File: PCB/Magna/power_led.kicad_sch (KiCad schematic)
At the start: 10 parts

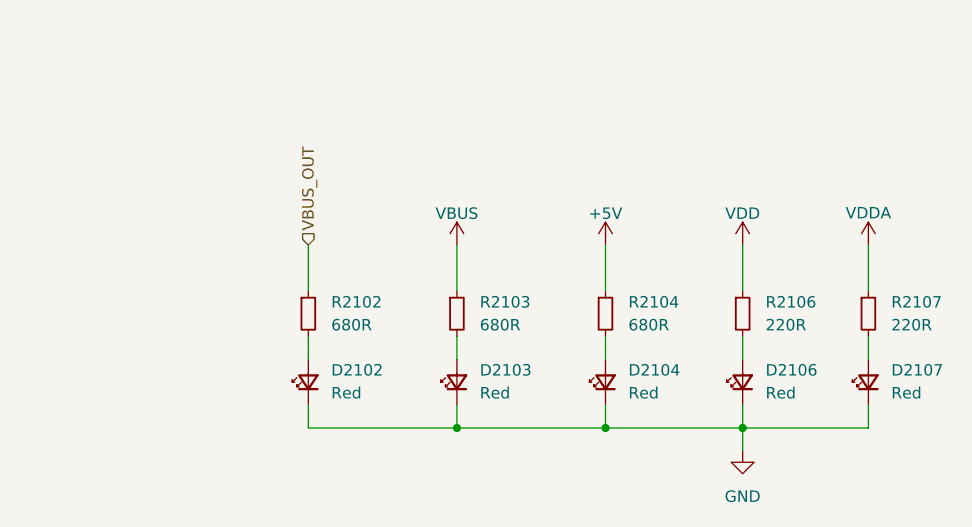
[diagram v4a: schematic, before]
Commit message: Mainboard layout (#19)
Also adds mounting holes to IO daughterboard
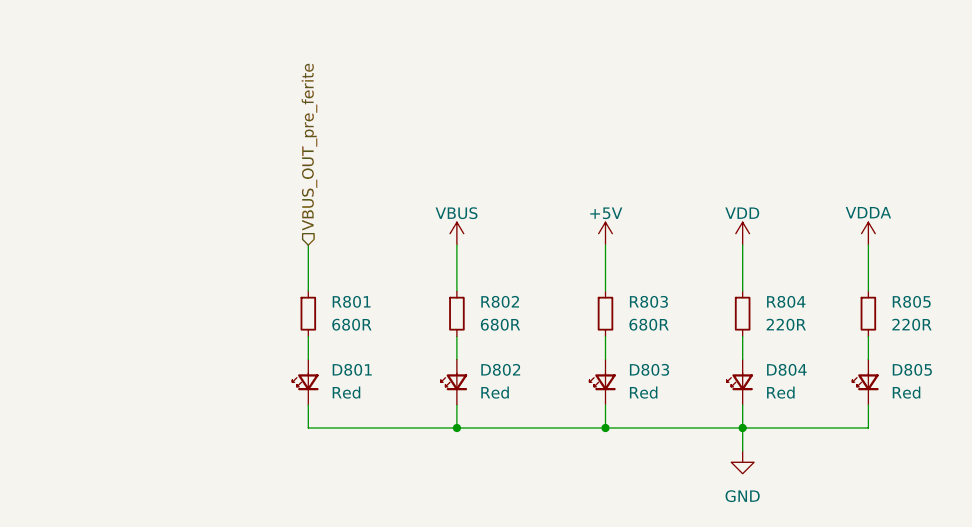
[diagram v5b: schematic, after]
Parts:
- renumbered D2102 to D801, D2103 to D802, D2104 to D803, D2106 to D804, D2107 to D805, R2102 to R801, R2103 to R802, R2104 to R803, R2106 to R804, R2107 to R805
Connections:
- net VBUS_OUT renamed VBUS_OUT_pre_ferite
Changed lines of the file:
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@@
     (stroke (width 0) (type default))
   )
-  (hierarchical_label "VBUS_OUT" (shape input) (at 93.98 54.61 90) (fields_autoplaced)
+  (hierarchical_label "VBUS_OUT_pre_ferite" (shape input) (at 93.98 54.61 90) (fields_autoplaced)
     (effects (font (size 1.27 1.27)) (justify left))
   )
   (symbol (lib_id "power:+5V") (at 127 54.61 0) (unit 1)
     (in_bom yes) (on_board yes) (dnp no) (fields_autoplaced)
-    (property "Reference" "#PWR02102" (at 127 58.42 0)
+    (property "Reference" "#PWR0802" (at 127 58.42 0)
       (effects (font (size 1.27 1.27)) hide)
     )
@@
       (project "Magna"
         (path "/1469ea1f-a157-49dc-a369-2d42fa17695d/b088328e-b490-4b17-95e1-21a9080368b1/8f3bd938-8820-47e0-9876-2fc55897716e"
-          (reference "#PWR02102") (unit 1)
+          (reference "#PWR0802") (unit 1)
         )
       )
@@
   (symbol (lib_id "Device:R_Small") (at 110.49 62.23 0) (unit 1)
     (in_bom yes) (on_board yes) (dnp no) (fields_autoplaced)
-    (property "Reference" "R2103" (at 113.03 60.96 0)
+    (property "Reference" "R802" (at 113.03 60.96 0)
       (effects (font (size 1.27 1.27)) (justify left))
     )
@@
       (project "Magna"
         (path "/1469ea1f-a157-49dc-a369-2d42fa17695d/b088328e-b490-4b17-95e1-21a9080368b1/8f3bd938-8820-47e0-9876-2fc55897716e"
-          (reference "R2103") (unit 1)
+          (reference "R802") (unit 1)
         )
       )
@@
   (symbol (lib_id "Device:LED_Small") (at 127 69.85 90) (unit 1)
     (in_bom yes) (on_board yes) (dnp no) (fields_autoplaced)
-    (property "Reference" "D2104" (at 129.54 68.5165 90)
+    (property "Reference" "D803" (at 129.54 68.5165 90)
       (effects (font (size 1.27 1.27)) (justify right))
     )
@@
       (project "Magna"
         (path "/1469ea1f-a157-49dc-a369-2d42fa17695d/b088328e-b490-4b17-95e1-21a9080368b1/8f3bd938-8820-47e0-9876-2fc55897716e"
-          (reference "D2104") (unit 1)
+          (reference "D803") (unit 1)
         )
       )
@@
   (symbol (lib_id "power:VDDA") (at 156.21 54.61 0) (unit 1)
     (in_bom yes) (on_board yes) (dnp no)
-    (property "Reference" "#PWR02106" (at 156.21 58.42 0)
+    (property "Reference" "#PWR0805" (at 156.21 58.42 0)
       (effects (font (size 1.27 1.27)) hide)
     )
@@
       (project "Magna"
         (path "/1469ea1f-a157-49dc-a369-2d42fa17695d/b088328e-b490-4b17-95e1-21a9080368b1/8f3bd938-8820-47e0-9876-2fc55897716e"
-          (reference "#PWR02106") (unit 1)
+          (reference "#PWR0805") (unit 1)
         )
       )
@@
   (symbol (lib_id "power:VBUS") (at 110.49 54.61 0) (unit 1)
     (in_bom yes) (on_board yes) (dnp no) (fields_autoplaced)
-    (property "Reference" "#PWR02101" (at 110.49 58.42 0)
+    (property "Reference" "#PWR0801" (at 110.49 58.42 0)
       (effects (font (size 1.27 1.27)) hide)
     )
@@
       (project "Magna"
         (path "/1469ea1f-a157-49dc-a369-2d42fa17695d/b088328e-b490-4b17-95e1-21a9080368b1/8f3bd938-8820-47e0-9876-2fc55897716e"
-          (reference "#PWR02101") (unit 1)
+          (reference "#PWR0801") (unit 1)
         )
       )
@@
   (symbol (lib_id "Device:LED_Small") (at 93.98 69.85 90) (unit 1)
     (in_bom yes) (on_board yes) (dnp no) (fields_autoplaced)
-    (property "Reference" "D2102" (at 96.52 68.5165 90)
+    (property "Reference" "D801" (at 96.52 68.5165 90)
       (effects (font (size 1.27 1.27)) (justify right))
     )
@@
       (project "Magna"
         (path "/1469ea1f-a157-49dc-a369-2d42fa17695d/b088328e-b490-4b17-95e1-21a9080368b1/8f3bd938-8820-47e0-9876-2fc55897716e"
-          (reference "D2102") (unit 1)
+          (reference "D801") (unit 1)
         )
       )
@@
   (symbol (lib_id "Device:LED_Small") (at 110.49 69.85 90) (unit 1)
     (in_bom yes) (on_board yes) (dnp no) (fields_autoplaced)
-    (property "Reference" "D2103" (at 113.03 68.5165 90)
+    (property "Reference" "D802" (at 113.03 68.5165 90)
       (effects (font (size 1.27 1.27)) (justify right))
     )
@@
       (project "Magna"
         (path "/1469ea1f-a157-49dc-a369-2d42fa17695d/b088328e-b490-4b17-95e1-21a9080368b1/8f3bd938-8820-47e0-9876-2fc55897716e"
-          (reference "D2103") (unit 1)
+          (reference "D802") (unit 1)
         )
       )
@@
   (symbol (lib_id "Device:R_Small") (at 127 62.23 0) (unit 1)
     (in_bom yes) (on_board yes) (dnp no) (fields_autoplaced)
-    (property "Reference" "R2104" (at 129.54 60.96 0)
+    (property "Reference" "R803" (at 129.54 60.96 0)
       (effects (font (size 1.27 1.27)) (justify left))
     )
@@
       (project "Magna"
         (path "/1469ea1f-a157-49dc-a369-2d42fa17695d/b088328e-b490-4b17-95e1-21a9080368b1/8f3bd938-8820-47e0-9876-2fc55897716e"
-          (reference "R2104") (unit 1)
+          (reference "R803") (unit 1)
         )
       )
@@
   (symbol (lib_id "Device:LED_Small") (at 142.24 69.85 90) (unit 1)
     (in_bom yes) (on_board yes) (dnp no) (fields_autoplaced)
-    (property "Reference" "D2106" (at 144.78 68.5165 90)
+    (property "Reference" "D804" (at 144.78 68.5165 90)
       (effects (font (size 1.27 1.27)) (justify right))
     )
@@
       (project "Magna"
         (path "/1469ea1f-a157-49dc-a369-2d42fa17695d/b088328e-b490-4b17-95e1-21a9080368b1/8f3bd938-8820-47e0-9876-2fc55897716e"
-          (reference "D2106") (unit 1)
+          (reference "D804") (unit 1)
         )
       )
@@
   (symbol (lib_id "Device:R_Small") (at 93.98 62.23 0) (unit 1)
     (in_bom yes) (on_board yes) (dnp no) (fields_autoplaced)
-    (property "Reference" "R2102" (at 96.52 60.96 0)
+    (property "Reference" "R801" (at 96.52 60.96 0)
       (effects (font (size 1.27 1.27)) (justify left))
     )
@@
       (project "Magna"
         (path "/1469ea1f-a157-49dc-a369-2d42fa17695d/b088328e-b490-4b17-95e1-21a9080368b1/8f3bd938-8820-47e0-9876-2fc55897716e"
-          (reference "R2102") (unit 1)
+          (reference "R801") (unit 1)
         )
       )
@@
   (symbol (lib_id "power:GND") (at 142.24 77.47 0) (unit 1)
     (in_bom yes) (on_board yes) (dnp no) (fields_autoplaced)
-    (property "Reference" "#PWR02105" (at 142.24 83.82 0)
+    (property "Reference" "#PWR0804" (at 142.24 83.82 0)
       (effects (font (size 1.27 1.27)) hide)
     )
@@
       (project "Magna"
         (path "/1469ea1f-a157-49dc-a369-2d42fa17695d/b088328e-b490-4b17-95e1-21a9080368b1/8f3bd938-8820-47e0-9876-2fc55897716e"
-          (reference "#PWR02105") (unit 1)
+          (reference "#PWR0804") (unit 1)
         )
       )
@@
   (symbol (lib_id "Device:R_Small") (at 156.21 62.23 0) (unit 1)
     (in_bom yes) (on_board yes) (dnp no) (fields_autoplaced)
-    (property "Reference" "R2107" (at 158.75 60.96 0)
+    (property "Reference" "R805" (at 158.75 60.96 0)
       (effects (font (size 1.27 1.27)) (justify left))
     )
@@
       (project "Magna"
         (path "/1469ea1f-a157-49dc-a369-2d42fa17695d/b088328e-b490-4b17-95e1-21a9080368b1/8f3bd938-8820-47e0-9876-2fc55897716e"
-          (reference "R2107") (unit 1)
+          (reference "R805") (unit 1)
         )
       )
@@
   (symbol (lib_id "Device:LED_Small") (at 156.21 69.85 90) (unit 1)
     (in_bom yes) (on_board yes) (dnp no) (fields_autoplaced)
-    (property "Reference" "D2107" (at 158.75 68.5165 90)
+    (property "Reference" "D805" (at 158.75 68.5165 90)
       (effects (font (size 1.27 1.27)) (justify right))
     )
@@
       (project "Magna"
         (path "/1469ea1f-a157-49dc-a369-2d42fa17695d/b088328e-b490-4b17-95e1-21a9080368b1/8f3bd938-8820-47e0-9876-2fc55897716e"
-          (reference "D2107") (unit 1)
+          (reference "D805") (unit 1)
         )
       )
@@
   (symbol (lib_id "Device:R_Small") (at 142.24 62.23 0) (unit 1)
     (in_bom yes) (on_board yes) (dnp no) (fields_autoplaced)
-    (property "Reference" "R2106" (at 144.78 60.96 0)
+    (property "Reference" "R804" (at 144.78 60.96 0)
       (effects (font (size 1.27 1.27)) (justify left))
     )
@@
       (project "Magna"
         (path "/1469ea1f-a157-49dc-a369-2d42fa17695d/b088328e-b490-4b17-95e1-21a9080368b1/8f3bd938-8820-47e0-9876-2fc55897716e"
-          (reference "R2106") (unit 1)
+          (reference "R804") (unit 1)
         )
       )
@@
   (symbol (lib_id "power:VDD") (at 142.24 54.61 0) (unit 1)
     (in_bom yes) (on_board yes) (dnp no)
-    (property "Reference" "#PWR02104" (at 142.24 58.42 0)
+    (property "Reference" "#PWR0803" (at 142.24 58.42 0)
       (effects (font (size 1.27 1.27)) hide)
     )
@@
       (project "Magna"
         (path "/1469ea1f-a157-49dc-a369-2d42fa17695d/b088328e-b490-4b17-95e1-21a9080368b1/8f3bd938-8820-47e0-9876-2fc55897716e"
-          (reference "#PWR02104") (unit 1)
-        )
-      )
+          (reference "#PWR0803") (unit 1)
+        )
+      )

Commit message: Some updates to PCB
Honestly I cannot remember whats changed
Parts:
- R801, R802, R803: LCSC C865612 -> C17798
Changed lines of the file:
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@@
 			)
 		)
-		(property "LCSC" "C865612"
+		(property "LCSC" "C17798"
 			(at 110.49 62.23 0)
 			(effects
@@
 			)
 		)
-		(property "LCSC" "C865612"
+		(property "LCSC" "C17798"
 			(at 127 62.23 0)
 			(effects
@@
 			)
 		)
-		(property "LCSC" "C865612"
+		(property "LCSC" "C17798"
 			(at 93.98 62.23 0)
 			(effects
